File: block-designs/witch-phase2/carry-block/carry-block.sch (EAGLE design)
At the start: 12 parts, among them IC1 74AHC1G32DBV, IC2 74AHC1G08DBV, IC3 74175-S

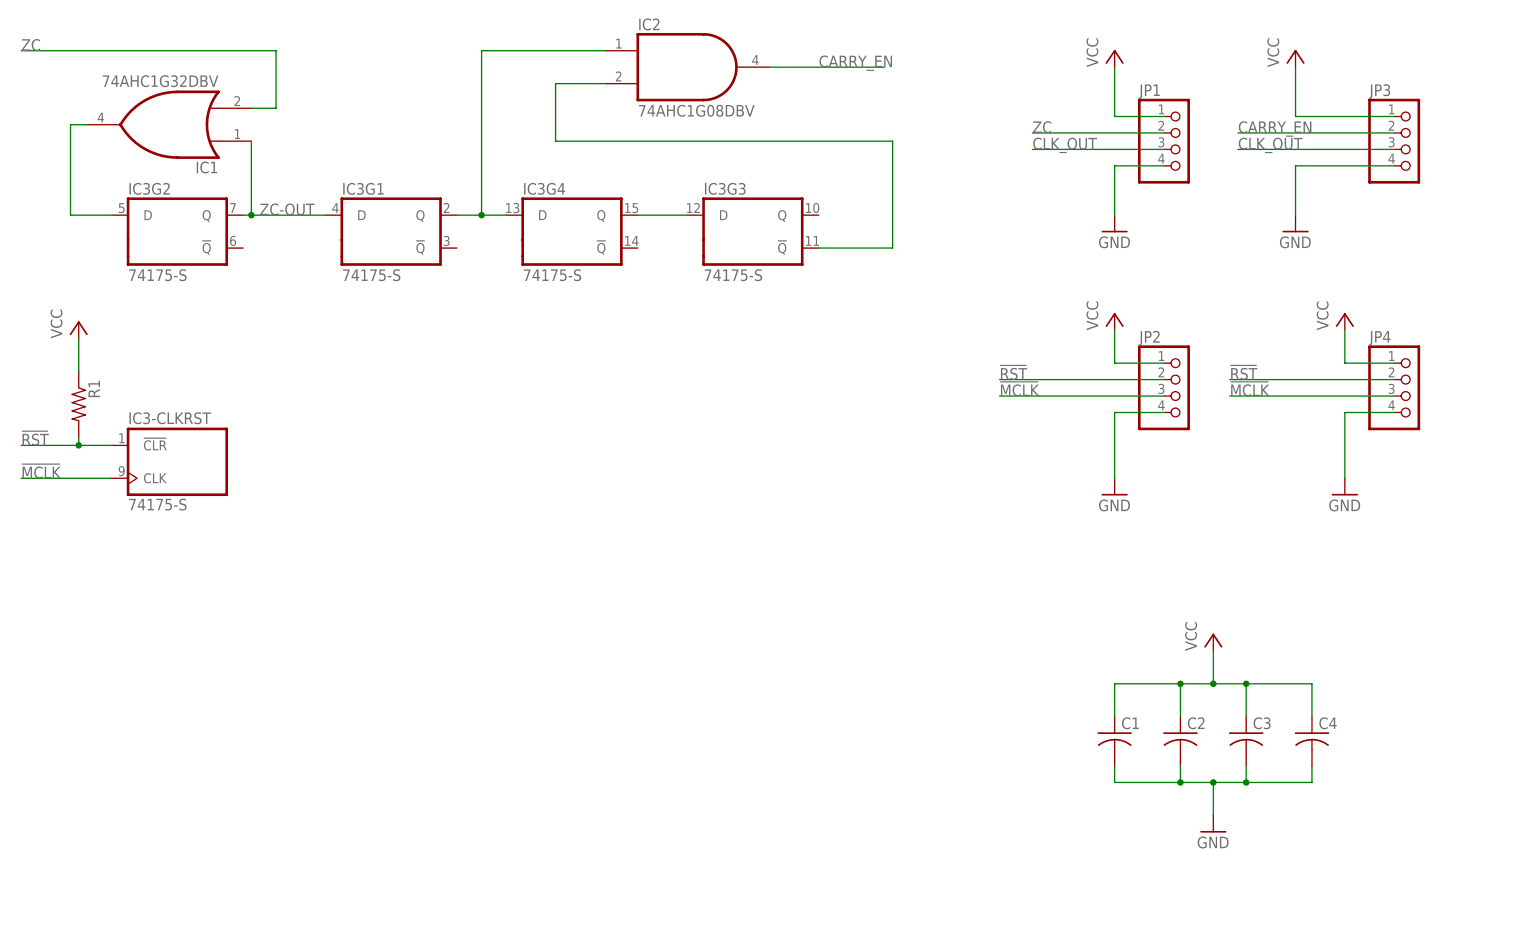
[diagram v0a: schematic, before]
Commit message: updated with 74hc195 and carry_oe signal
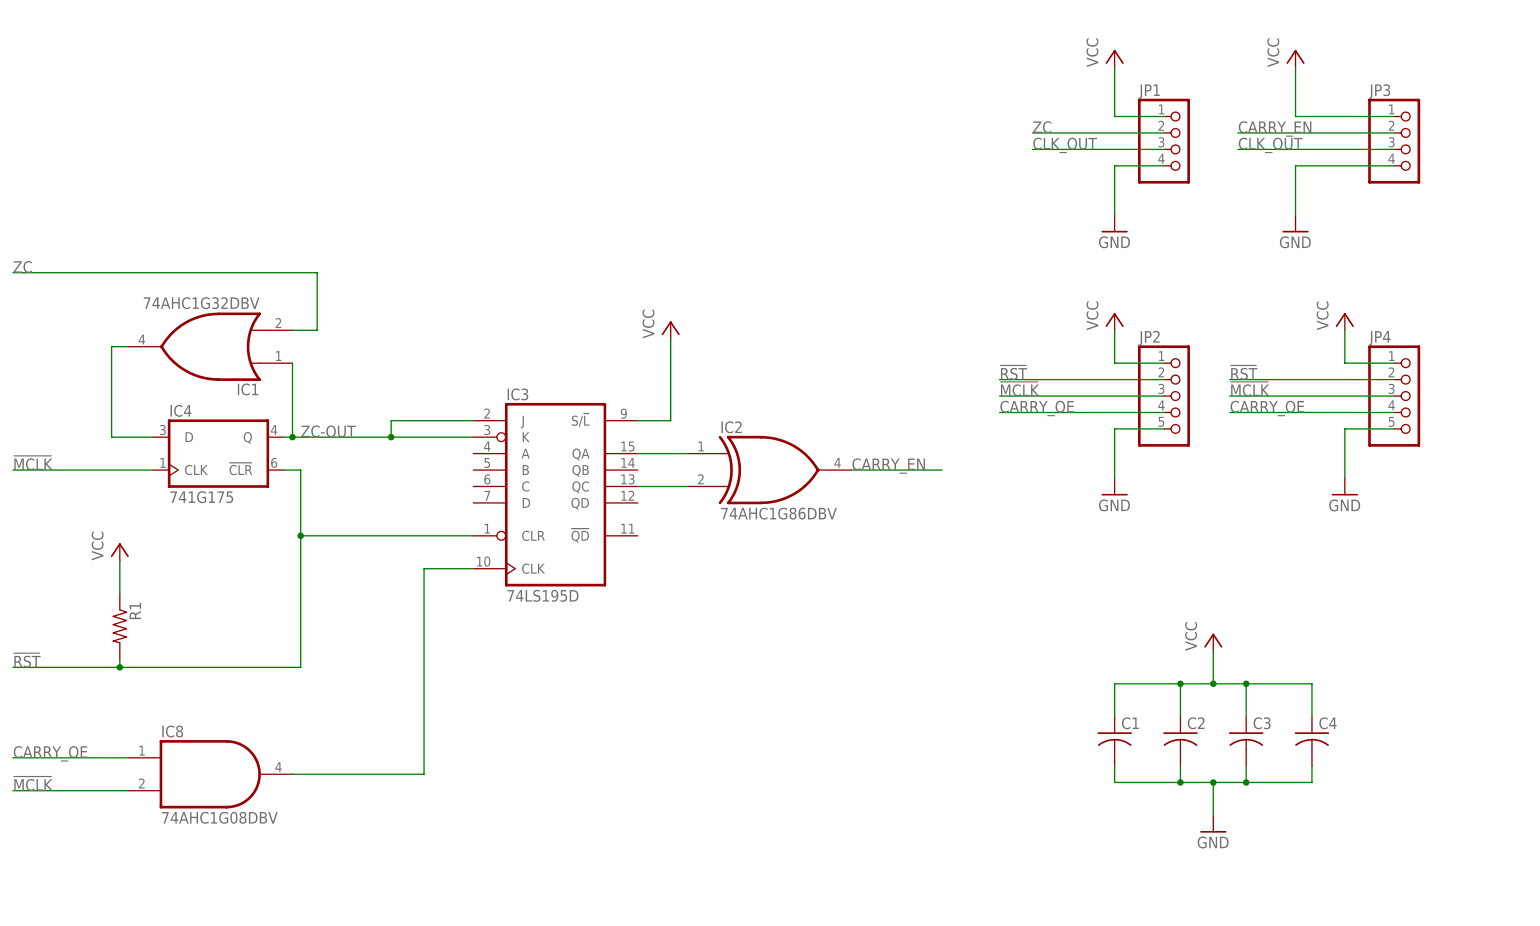
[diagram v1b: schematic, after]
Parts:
- added IC4: 741G175, 74xx-little-us:741G175
- added IC8: 74AHC1G08DBV, 74xx-little-us:74AHC1G08DBV
- IC2: value 74AHC1G08DBV -> 74AHC1G86DBV; device 74xx-little-us:74AHC1G08DBV -> 74xx-little-us:74AHC1G86DBV
- IC3: value 74175-S -> 74LS195D; device 74xx-us:74175-S -> 74xx-us:74LS195D
- JP2, JP4: device pinhead:PINHD-1X4 -> pinhead:PINHD-1X5
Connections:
- new net CARRY_OE: IC8A.I0, JP2.4, JP4.4
- net !MCLK: now also IC4G$1.CLK, IC8A.I1; no longer IC3-CLKRST.CLK
- net !RST: now also IC3A.CLR, IC4G$1.!CLR; no longer IC3-CLKRST.!CLR
- net GND: now also JP2.5, JP4.5; no longer JP2.4, JP4.4
- net N$1: now also IC3A.QA; no longer IC3G1.Q, IC3G4.D
- net N$2: now also IC3A.QC; no longer IC3G3.!Q
- net N$3: now also IC3A.CLK, IC8A.O; no longer IC3G3.D, IC3G4.Q
- net N$5: now also IC4G$1.D; no longer IC3G2.D
- net VCC: now also IC3A.S/!L
- net ZC-OUT: now also IC3A.J, IC3A.K, IC4G$1.Q; no longer IC3G1.D, IC3G2.Q
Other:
- moved on the sheet: IC1, R1

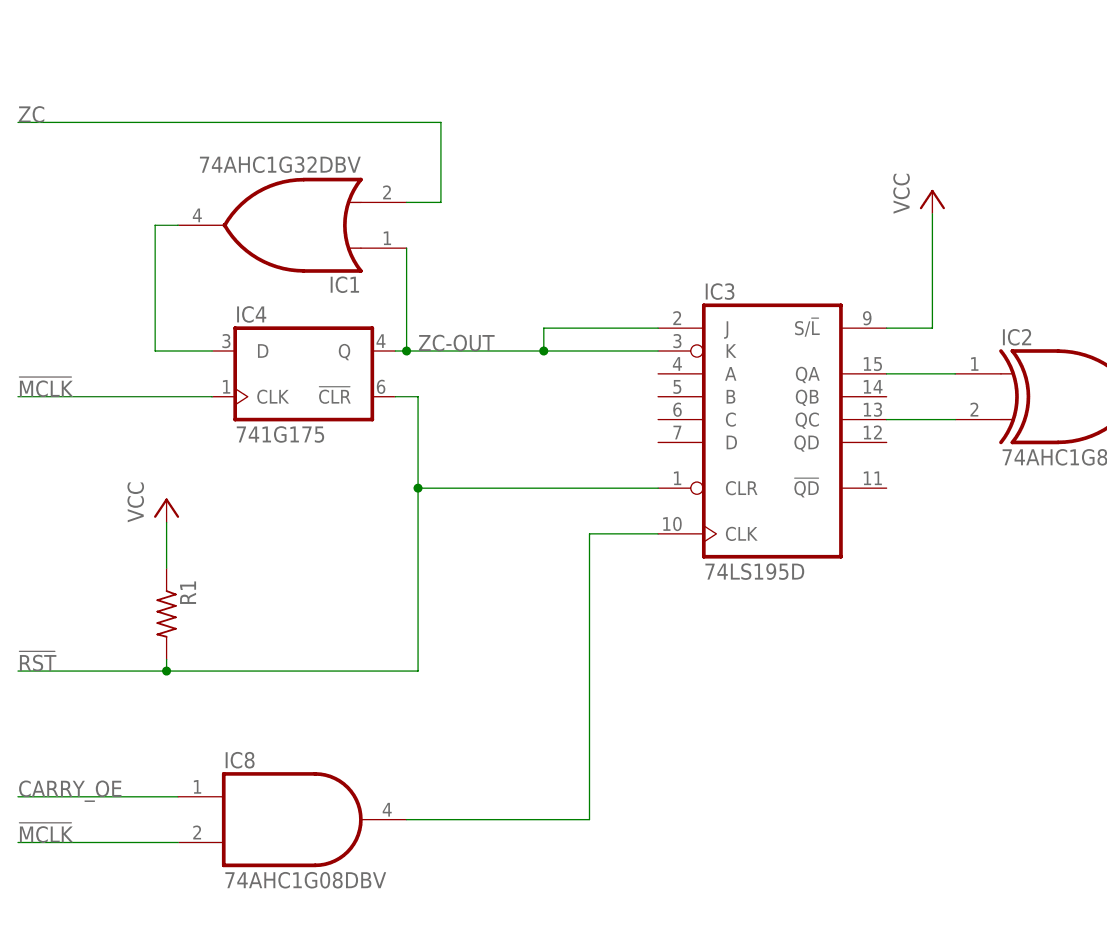
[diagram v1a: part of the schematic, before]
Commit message: remove AND gate and use the Set/Load function
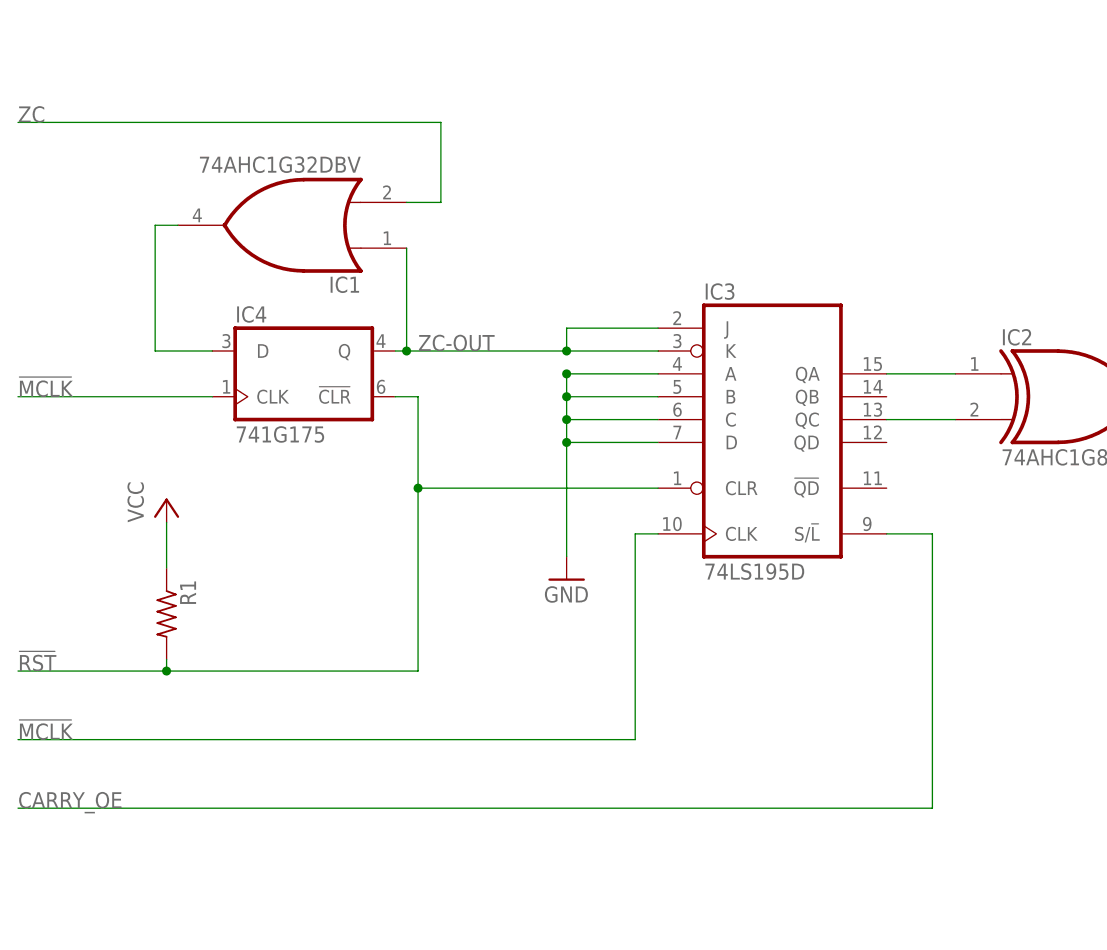
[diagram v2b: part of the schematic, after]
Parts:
- removed IC8: 74AHC1G08DBV, 74xx-little-us:74AHC1G08DBV
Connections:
- removed net N$3: IC3A.CLK, IC8A.O
- net !MCLK: now also IC3A.CLK; no longer IC8A.I1
- net CARRY_OE: now also IC3A.S/!L; no longer IC8A.I0
- net GND: now also IC3A.A, IC3A.B, IC3A.C, IC3A.D
- net VCC: no longer IC3A.S/!L
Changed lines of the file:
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@@
 <part name="P+6" library="supply1" deviceset="VCC" device=""/>
 <part name="IC4" library="74xx-little-us" deviceset="74*1G175" device=""/>
-<part name="IC8" library="74xx-little-us" deviceset="74*1G08" device="DBV" technology="AHC"/>
 <part name="IC2" library="74xx-little-us" deviceset="74*1G86" device="DBV" technology="AHC"/>
 <part name="IC3" library="74xx-us" deviceset="74*195" device="D" technology="LS"/>
-<part name="P+7" library="supply1" deviceset="VCC" device=""/>
+<part name="GND6" library="supply1" deviceset="GND" device=""/>
 </parts>
 <sheets>
@@
 <instance part="P+6" gate="VCC" x="25.4" y="100.33"/>
 <instance part="IC4" gate="G$1" x="38.1" y="114.3"/>
-<instance part="IC8" gate="A" x="39.37" y="64.77"/>
 <instance part="IC2" gate="A" x="125.73" y="111.76"/>
 <instance part="IC3" gate="A" x="92.71" y="109.22"/>
-<instance part="P+7" gate="VCC" x="110.49" y="134.62"/>
+<instance part="GND6" gate="1" x="69.85" y="91.44"/>
 </instances>
 <busses>
@@
 <wire x1="214.63" y1="118.11" x2="214.63" y2="110.49" width="0.1524" layer="91"/>
 </segment>
+<segment>
+<pinref part="IC3" gate="A" pin="A"/>
+<wire x1="80.01" y1="114.3" x2="69.85" y2="114.3" width="0.1524" layer="91"/>
+<wire x1="69.85" y1="114.3" x2="69.85" y2="111.76" width="0.1524" layer="91"/>
+<pinref part="IC3" gate="A" pin="B"/>
+<wire x1="69.85" y1="111.76" x2="69.85" y2="109.22" width="0.1524" layer="91"/>
+<wire x1="69.85" y1="109.22" x2="69.85" y2="106.68" width="0.1524" layer="91"/>
+<wire x1="69.85" y1="106.68" x2="69.85" y2="93.98" width="0.1524" layer="91"/>
+<wire x1="80.01" y1="111.76" x2="69.85" y2="111.76" width="0.1524" layer="91"/>
+<pinref part="IC3" gate="A" pin="C"/>
+<wire x1="80.01" y1="109.22" x2="69.85" y2="109.22" width="0.1524" layer="91"/>
+<pinref part="IC3" gate="A" pin="D"/>
+<wire x1="80.01" y1="106.68" x2="69.85" y2="106.68" width="0.1524" layer="91"/>
+<junction x="69.85" y="114.3"/>
+<junction x="69.85" y="111.76"/>
+<junction x="69.85" y="109.22"/>
+<junction x="69.85" y="106.68"/>
+<pinref part="GND6" gate="1" pin="GND"/>
+</segment>
 </net>
 <net name="VCC" class="0">
@@
 <wire x1="25.4" y1="92.71" x2="25.4" y2="97.79" width="0.1524" layer="91"/>
 </segment>
-<segment>
-<pinref part="IC3" gate="A" pin="S/!L"/>
-<wire x1="105.41" y1="119.38" x2="110.49" y2="119.38" width="0.1524" layer="91"/>
-<wire x1="110.49" y1="119.38" x2="110.49" y2="132.08" width="0.1524" layer="91"/>
-<pinref part="P+7" gate="VCC" pin="VCC"/>
-</segment>
 </net>
 <net name="ZC" class="0">
@@
 <pinref part="IC4" gate="G$1" pin="Q"/>
 <pinref part="IC3" gate="A" pin="K"/>
-<wire x1="80.01" y1="116.84" x2="67.31" y2="116.84" width="0.1524" layer="91"/>
+<wire x1="80.01" y1="116.84" x2="69.85" y2="116.84" width="0.1524" layer="91"/>
 <pinref part="IC3" gate="A" pin="J"/>
-<wire x1="67.31" y1="116.84" x2="52.07" y2="116.84" width="0.1524" layer="91"/>
-<wire x1="80.01" y1="119.38" x2="67.31" y2="119.38" width="0.1524" layer="91"/>
-<wire x1="67.31" y1="119.38" x2="67.31" y2="116.84" width="0.1524" layer="91"/>
-<junction x="67.31" y="116.84"/>
+<wire x1="69.85" y1="116.84" x2="52.07" y2="116.84" width="0.1524" layer="91"/>
+<wire x1="80.01" y1="119.38" x2="69.85" y2="119.38" width="0.1524" layer="91"/>
+<wire x1="69.85" y1="119.38" x2="69.85" y2="116.84" width="0.1524" layer="91"/>
+<junction x="69.85" y="116.84"/>
 </segment>
 </net>
@@
 </segment>
 <segment>
-<pinref part="IC8" gate="A" pin="I1"/>
-<wire x1="26.67" y1="62.23" x2="8.89" y2="62.23" width="0.1524" layer="91"/>
-<label x="8.89" y="62.23" size="1.778" layer="95"/>
+<label x="8.89" y="73.66" size="1.778" layer="95"/>
+<wire x1="77.47" y1="73.66" x2="8.89" y2="73.66" width="0.1524" layer="91"/>
+<wire x1="77.47" y1="73.66" x2="77.47" y2="96.52" width="0.1524" layer="91"/>
+<pinref part="IC3" gate="A" pin="CLK"/>
+<wire x1="77.47" y1="96.52" x2="80.01" y2="96.52" width="0.1524" layer="91"/>
 </segment>
 </net>
@@
 </segment>
 <segment>
-<wire x1="26.67" y1="67.31" x2="8.89" y2="67.31" width="0.1524" layer="91"/>
-<label x="8.89" y="67.31" size="1.778" layer="95"/>
-<pinref part="IC8" gate="A" pin="I0"/>
-</segment>
-</net>
-<net name="N$3" class="0">
-<segment>
-<pinref part="IC8" gate="A" pin="O"/>
-<wire x1="72.39" y1="64.77" x2="52.07" y2="64.77" width="0.1524" layer="91"/>
-<wire x1="72.39" y1="64.77" x2="72.39" y2="96.52" width="0.1524" layer="91"/>
-<pinref part="IC3" gate="A" pin="CLK"/>
-<wire x1="72.39" y1="96.52" x2="80.01" y2="96.52" width="0.1524" layer="91"/>
-</segment>
-</net>
+<wire x1="8.89" y1="66.04" x2="110.49" y2="66.04" width="0.1524" layer="91"/>
+<wire x1="110.49" y1="66.04" x2="110.49" y2="96.52" width="0.1524" layer="91"/>
+<pinref part="IC3" gate="A" pin="S/!L"/>
+<wire x1="110.49" y1="96.52" x2="105.41" y2="96.52" width="0.1524" layer="91"/>
+<label x="8.89" y="66.04" size="1.778" layer="95"/>
+</segment>
+</net>
